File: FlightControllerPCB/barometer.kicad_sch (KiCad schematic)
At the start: 0 parts

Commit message: barometer schematic
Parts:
- added C1, C6: 100nF, symbol Device:C_Small
- added R1: 10k, symbol Device:R_Small
- added R7, R8: 4.7k, symbol Device:R_Small
- added U3: BMP388, BMP388:XDCR_BMP388, symbol BMP388:BMP388
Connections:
- new net: R1.2, U3.6 (CSB)
- new net +3.3V: C1.1, C6.2, R1.1, R7.1, R8.1, U3.1 (VDDIO), U3.10 (VDD)
- new net BARO_INT: U3.7 (INT)
- new net GND: C1.2, C6.1, U3.3 (VSS), U3.5 (SDO), U3.8 (VSS), U3.9 (VSS)
- new net I2C1_SCK: R8.2, U3.2 (SCK)
- new net I2C1_SDI: R7.2, U3.4 (SDI)
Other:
- note added: "8 pins on footprint vs 10 pins (8/9 are GND)"
- note added: "Looks way different than symbols on Adafruit schematic"
- note added: "Not sure what is up in the top right corner with the capicators/GNDs"
- note added: "Notes for rohith to look over:"

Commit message: some edits
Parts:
- removed C1, C6: 100nF, symbol Device:C_Small
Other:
- moved on the sheet: R1, R7, R8

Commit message: Hella sheets
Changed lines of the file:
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@@
 		(in_pos_files yes)
 		(dnp no)
-		(fields_autoplaced yes)
 		(property "Reference" "R8"
-			(at 118.11 99.0599 0)
+			(at 117.602 99.06 0)
 			(show_name no)
 			(do_not_autoplace no)
@@
 		)
 		(property "Value" "4.7k"
-			(at 118.11 101.5999 0)
+			(at 117.602 101.6 0)
 			(show_name no)
 			(do_not_autoplace no)
@@
 		(in_pos_files yes)
 		(dnp no)
-		(fields_autoplaced yes)
 		(property "Reference" "R7"
-			(at 113.03 127.0001 0)
+			(at 121.412 127.254 0)
 			(show_name no)
 			(do_not_autoplace no)
@@
 		)
 		(property "Value" "4.7k"
-			(at 113.03 124.4601 0)
+			(at 121.412 124.714 0)
 			(show_name no)
 			(do_not_autoplace no)

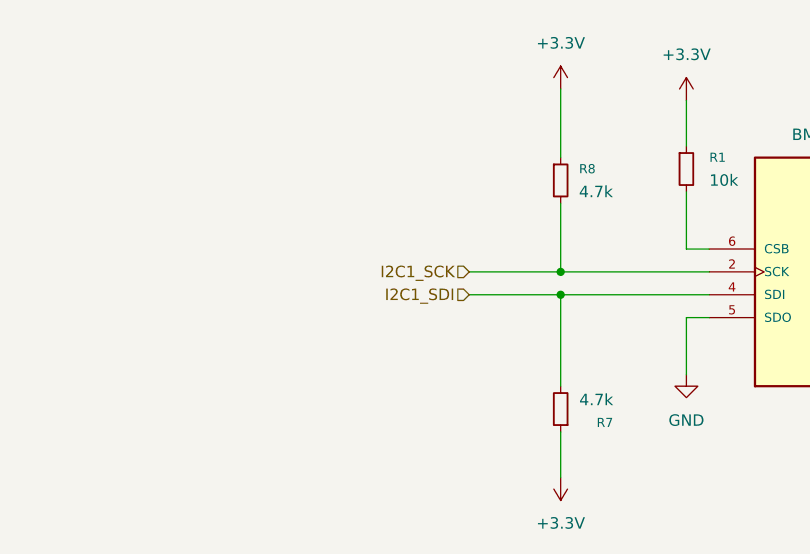
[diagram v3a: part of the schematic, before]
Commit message: initial baro/imu to mcu pins
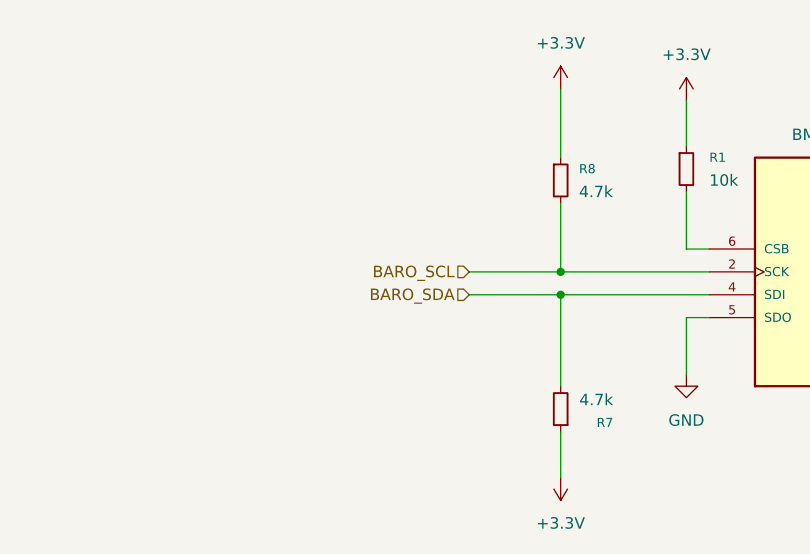
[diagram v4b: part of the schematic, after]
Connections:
- net I2C1_SCK renamed BARO_SCL
- net I2C1_SDI renamed BARO_SDA
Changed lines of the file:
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@@
 		)
 	)
-	(hierarchical_label "I2C1_SDI"
+	(hierarchical_label "BARO_SDA"
 		(shape input)
 		(at 105.41 113.03 180)
@@
 		)
 	)
-	(hierarchical_label "I2C1_SCK"
+	(hierarchical_label "BARO_SCL"
 		(shape input)
 		(at 105.41 110.49 180)

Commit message: actually the IMU+baro changes
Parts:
- added C1, C14: .1uF, symbol Device:C
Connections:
- net +3.3V: now also C1.1, C14.1
- net GND: now also C1.2, C14.2

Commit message: Power circuit
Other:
- note added: "- MOSFET+Pull ups??? - quick AI circuit check"
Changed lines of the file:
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@@
+		)
+	)
+	(text "- MOSFET+Pull ups???\n- quick AI circuit check"
+		(exclude_from_sim no)
+		(at 221.742 61.722 0)
+		(effects
+			(font
+				(size 2.54 2.54)
+			)
 		)
 	)

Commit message: early MCU setup
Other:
- note added: "- MOSFET+Pull ups??? - Sanity Check"
- note removed: "- MOSFET+Pull ups??? - quick AI circuit check"
- note removed: "8 pins on footprint vs 10 pins (8/9 are GND)"
- note removed: "Looks way different than symbols on Adafruit schematic"
- note removed: "Not sure what is up in the top right corner with the capicators/GNDs"
- note removed: "Notes for rohith to look over:"
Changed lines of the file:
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@@
 	(generator_version "10.0")
 	(paper "A4")
-	(text "8 pins on footprint vs 10 pins (8/9 are GND)\n"
-		(exclude_from_sim no)
-		(at 44.196 32.512 0)
-		(effects
-			(font
-				(size 1.27 1.27)
-			)
-		)
-	)
-	(text "- MOSFET+Pull ups???\n- quick AI circuit check"
+	(text "- MOSFET+Pull ups???\n- Sanity Check"
 		(exclude_from_sim no)
 		(at 221.742 61.722 0)
@@
 			)
 		)
-	)
-	(text "Looks way different than symbols on Adafruit schematic\n"
-		(exclude_from_sim no)
-		(at 48.768 38.608 0)
-		(effects
-			(font
-				(size 1.27 1.27)
-			)
-		)
-	)
-	(text "Not sure what is up in the top right corner with the capicators/GNDs\n\n"
-		(exclude_from_sim no)
-		(at 55.372 45.212 0)
-		(effects
-			(font
-				(size 1.27 1.27)
-			)
-		)
-	)
-	(text "Notes for rohith to look over:\n"
-		(exclude_from_sim no)
-		(at 30.226 22.098 0)
-		(effects
-			(font
-				(size 1.27 1.27)
-			)
-		)

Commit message: Sanity check+Error fixes
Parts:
- added C15: .1uF, symbol Device:C
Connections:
- net GND: now also C15.2; no longer U3.3 (VSS), U3.8 (VSS), U3.9 (VSS)
- new net VSS: C15.1, U3.3 (VSS), U3.8 (VSS), U3.9 (VSS)
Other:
- note removed: "- MOSFET+Pull ups??? - Sanity Check"
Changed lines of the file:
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@@
 	(generator_version "10.0")
 	(paper "A4")
-	(text "- MOSFET+Pull ups???\n- Sanity Check"
-		(exclude_from_sim no)
-		(at 221.742 61.722 0)
-		(effects
-			(font
-				(size 2.54 2.54)
-			)
-		)
+	(junction
+		(at 166.37 120.65)
+		(diameter 0)
+		(color 0 0 0 0)
 	)
 	(junction
@@
 	(wire
 		(pts
-			(xy 166.37 120.65) (xy 166.37 123.19)
-		)
-		(stroke
-			(width 0)
-			(type default)
-		)
-	)
-	(wire
-		(pts
 			(xy 161.29 100.33) (xy 161.29 88.9)
 		)
@@
 		(pts
 			(xy 168.91 88.9) (xy 181.61 88.9)
-		)
-		(stroke
-			(width 0)
-			(type default)
-		)
-	)
-	(wire
-		(pts
-			(xy 157.48 110.49) (xy 166.37 110.49)
 		)
 		(stroke
@@
 	(hierarchical_label "BARO_INT"
 		(shape input)
-		(at 166.37 110.49 0)
+		(at 157.48 110.49 0)
 		(effects
 			(font
@@
 	)
 	(symbol
+		(lib_id "power:GND")
+		(at 166.37 128.27 0)
+		(unit 1)
+		(body_style 1)
+		(exclude_from_sim no)
+		(in_bom yes)
+		(on_board yes)
+		(in_pos_files yes)
+		(dnp no)
+		(fields_autoplaced yes)
+		(property "Reference" "#PWR050"
+			(at 166.37 134.62 0)
+			(hide yes)
+			(show_name no)
+			(do_not_autoplace no)
+			(effects
+				(font
+					(size 1.27 1.27)
+				)
+			)
+		)
+		(property "Value" "GND"
+			(at 166.37 133.35 0)
+			(show_name no)
+			(do_not_autoplace no)
+			(effects
+				(font
+					(size 1.27 1.27)
+				)
+			)
+		)
+		(property "Footprint" ""
+			(at 166.37 128.27 0)
+			(hide yes)
+			(show_name no)
+			(do_not_autoplace no)
+			(effects
+				(font
+					(size 1.27 1.27)
+				)
+			)
+		)
+		(property "Datasheet" ""
+			(at 166.37 128.27 0)
+			(hide yes)
+			(show_name no)
+			(do_not_autoplace no)
+			(effects
+				(font
+					(size 1.27 1.27)
+				)
+			)
+		)
+		(property "Description" "Power symbol creates a global label with name \"GND\" , ground"
+			(at 166.37 128.27 0)
+			(hide yes)
+			(show_name no)
+			(do_not_autoplace no)
+			(effects
+				(font
+					(size 1.27 1.27)
+				)
+			)
+		)
+		(pin "1"
+		)
+		(instances
+			(project "FlightControllerPCB"
+				(path "/76f1a6d4-2c8f-4e0d-a089-f3ef3841ff54/65f93a8c-4278-43b1-9171-09686ed36ad0"
+					(reference "#PWR050")
+					(unit 1)
+				)
+			)
+		)
+	)
+	(symbol
 		(lib_id "power:+3.3V")
 		(at 129.54 91.44 0)
@@
 				(path "/76f1a6d4-2c8f-4e0d-a089-f3ef3841ff54/65f93a8c-4278-43b1-9171-09686ed36ad0"
 					(reference "#PWR020")
+					(unit 1)
+				)
+			)
+		)
+	)
+	(symbol
+		(lib_id "Device:C")
+		(at 166.37 124.46 0)
+		(unit 1)
+		(body_style 1)
+		(exclude_from_sim no)
+		(in_bom yes)
+		(on_board yes)
+		(in_pos_files yes)
+		(dnp no)
+		(fields_autoplaced yes)
+		(property "Reference" "C15"
+			(at 170.18 123.1899 0)
+			(show_name no)
+			(do_not_autoplace no)
+			(effects
+				(font
+					(size 1.27 1.27)
+				)
+				(justify left)
+			)
+		)
+		(property "Value" ".1uF"
+			(at 170.18 125.7299 0)
+			(show_name no)
+			(do_not_autoplace no)
+			(effects
+				(font
+					(size 1.27 1.27)
+				)
+				(justify left)
+			)
+		)
+		(property "Footprint" ""
+			(at 167.3352 128.27 0)
+			(hide yes)
+			(show_name no)
+			(do_not_autoplace no)
+			(effects
+				(font
+					(size 1.27 1.27)
+				)
+			)
+		)
+		(property "Datasheet" ""
+			(at 166.37 124.46 0)
+			(hide yes)
+			(show_name no)
+			(do_not_autoplace no)
+			(effects
+				(font
+					(size 1.27 1.27)
+				)
+			)
+		)
+		(property "Description" "Unpolarized capacitor"
+			(at 166.37 124.46 0)
+			(hide yes)
+			(show_name no)
+			(do_not_autoplace no)
+			(effects
+				(font
+					(size 1.27 1.27)
+				)
+			)
+		)
+		(pin "2"
+		)
+		(pin "1"
+		)
+		(instances
+			(project "FlightControllerPCB"
+				(path "/76f1a6d4-2c8f-4e0d-a089-f3ef3841ff54/65f93a8c-4278-43b1-9171-09686ed36ad0"
+					(reference "C15")
 					(unit 1)
 				)
@@
 	)
 	(symbol
-		(lib_id "power:GND")
-		(at 166.37 123.19 0)
-		(unit 1)
-		(body_style 1)
-		(exclude_from_sim no)
-		(in_bom yes)
-		(on_board yes)
-		(in_pos_files yes)
-		(dnp no)
-		(fields_autoplaced yes)
-		(property "Reference" "#PWR03"
-			(at 166.37 129.54 0)
-			(hide yes)
-			(show_name no)
-			(do_not_autoplace no)
-			(effects
-				(font
-					(size 1.27 1.27)
-				)
-			)
-		)
-		(property "Value" "GND"
-			(at 166.37 128.27 0)
-			(show_name no)
-			(do_not_autoplace no)
-			(effects
-				(font
-					(size 1.27 1.27)
-				)
-			)
-		)
-		(property "Footprint" ""
-			(at 166.37 123.19 0)
-			(hide yes)
-			(show_name no)
-			(do_not_autoplace no)
-			(effects
-				(font
-					(size 1.27 1.27)
-				)
-			)
-		)
-		(property "Datasheet" ""
-			(at 166.37 123.19 0)
-			(hide yes)
-			(show_name no)
-			(do_not_autoplace no)
-			(effects
-				(font
-					(size 1.27 1.27)
-				)
-			)
-		)
-		(property "Description" "Power symbol creates a global label with name \"GND\" , ground"
-			(at 166.37 123.19 0)
-			(hide yes)
-			(show_name no)
-			(do_not_autoplace no)
-			(effects
-				(font
-					(size 1.27 1.27)
-				)
-			)
-		)
-		(pin "1"
-		)
-		(instances
-			(project "FlightControllerPCB"
-				(path "/76f1a6d4-2c8f-4e0d-a089-f3ef3841ff54/65f93a8c-4278-43b1-9171-09686ed36ad0"
-					(reference "#PWR03")
-					(unit 1)
-				)
-			)
-		)
-	)
-	(symbol
 		(lib_id "Device:C")
 		(at 168.91 92.71 0)
@@
 					(unit 1)
 				)
+			)
+		)
+	)
+	(symbol
+		(lib_id "power:PWR_FLAG")
+		(at 166.37 120.65 0)
+		(unit 1)
+		(body_style 1)
+		(exclude_from_sim no)
+		(in_bom yes)
+		(on_board yes)
+		(in_pos_files yes)
+		(dnp no)
+		(fields_autoplaced yes)
+		(property "Reference" "#FLG01"
+			(at 166.37 118.745 0)
+			(hide yes)
+			(show_name no)
+			(do_not_autoplace no)
+			(effects
+				(font
+					(size 1.27 1.27)
+				)
+			)
+		)
+		(property "Value" "PWR_FLAG"
+			(at 166.37 115.57 0)
+			(show_name no)
+			(do_not_autoplace no)
+			(effects
+				(font
+					(size 1.27 1.27)
+				)
+			)
+		)
+		(property "Footprint" ""
+			(at 166.37 120.65 0)
+			(hide yes)
+			(show_name no)
+			(do_not_autoplace no)
+			(effects
+				(font
+					(size 1.27 1.27)
+				)
+			)
+		)
+		(property "Datasheet" ""
+			(at 166.37 120.65 0)
+			(hide yes)
+			(show_name no)
+			(do_not_autoplace no)
+			(effects
+				(font
+					(size 1.27 1.27)
+				)
+			)
+		)
+		(property "Description" "Special symbol for telling ERC where power comes from"
+			(at 166.37 120.65 0)
+			(hide yes)
+			(show_name no)
+			(do_not_autoplace no)
+			(effects
+				(font
+					(size 1.27 1.27)
+				)
+			)
+		)
+		(pin "1"
+		)
+		(instances
+			(project "FlightControllerPCB"
+				(path "/76f1a6d4-2c8f-4e0d-a089-f3ef3841ff54/65f93a8c-4278-43b1-9171-09686ed36ad0"
+					(reference "#FLG01")
+					(unit 1)
+				)
